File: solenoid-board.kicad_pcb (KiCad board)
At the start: 2 copper layers, 32.2 x 10.5 mm, 8 parts, among them J1 JST_PH, J2 0.1" header, Q1 FDN339AN

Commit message: Saved and quit kicad
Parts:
- moved D1 0.85 mm to (119.7, 106.2)
- moved C1 0.85 mm to (114.8, 106.5)
- moved G*** 0.85 mm to (113.5, 107.0)
- moved L1 0.85 mm to (122.5, 107.1)
- moved R1 0.81 mm to (108.9, 109.5)
- moved Q1 0.78 mm to (108.8, 104.9)
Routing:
- net GND: track 12.1 -> 9.70 mm
- net Net-(C1-Pad1): track 12.6 -> 14.7 mm
- net /FIRE!: track 5.46 -> 5.99 mm
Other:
- board size 32.2 x 10.5 mm -> 33 x 10.5 mm
- board text added: "git.io/pulsr"
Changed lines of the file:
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@@
   (general
     (thickness 1.6)
-    (drawings 11)
-    (tracks 29)
+    (drawings 12)
+    (tracks 26)
     (zones 0)
     (modules 8)
@@
   )
   (module graphics:kiwi10mm (layer B.Cu)
-    (at 112.7 107 180)
+    (at 113.55 107 180)
     (descr "Imported from kiwi.svg")
     (tags svg2mod)
@@
   )
   (module Capacitor_SMD:CP_Elec_6.3x5.4 (layer F.Cu)
-    (at 114 106.5 90)
+    (at 114.85 106.5 90)
     (descr "SMD capacitor, aluminum electrolytic, Panasonic C55, 6.3x5.4mm")
     (tags "capacitor electrolytic")
@@
   )
   (module Diode_SMD:D_SOD-123F (layer F.Cu)
-    (at 118.8 106.2 90)
+    (at 119.65 106.2 90)
     (descr D_SOD-123F)
     (tags D_SOD-123F)
@@
   )
   (module Connector_JST:JST_PH_S2B-PH-K_1x02_P2.00mm_Horizontal (layer F.Cu)
-    (at 121.7 107.1 90)
+    (at 122.55 107.1 90)
     (descr "JST PH series connector, S2B-PH-K (http://www.jst-mfg.com/product/pdf/eng/ePH.pdf), generated with kicad-footprint-generator")
     (tags "connector JST PH top entry")
@@
   )
   (module Package_TO_SOT_SMD:SOT-23_Handsoldering (layer F.Cu)
-    (at 108.3 105.5 90)
+    (at 108.8 104.9 90)
     (descr "SOT-23, Handsoldering")
     (tags SOT-23)
@@
   )
   (module Resistor_SMD:R_1206_3216Metric_Pad1.42x1.75mm_HandSolder (layer F.Cu)
-    (at 108.8 110.3 180)
+    (at 108.9 109.5 180)
     (descr "Resistor SMD 1206 (3216 Metric), square (rectangular) end terminal, IPC_7351 nominal with elongated pad for handsoldering. (Body size source: http://www.tortai-tech.com/upload/download/2011102023233369053.pdf), generated with kicad-footprint-generator")
     (tags "resistor handsolder")
     (attr smd)
-    (fp_text reference R1 (at 0 1.5) (layer F.SilkS)
-      (effects (font (size 1 1) (thickness 0.15)))
+    (fp_text reference R1 (at 0 1.4) (layer F.SilkS)
+      (effects (font (size 0.8 0.8) (thickness 0.13)))
     )
     (fp_text value 22R (at 0 1.82) (layer F.Fab)
@@
     )
   )
-  (gr_text Solenoid (at 121.4 102.9) (layer B.SilkS)
+  (gr_text git.io/pulsr (at 127.5 110) (layer B.SilkS)
+    (effects (font (size 1.25 1.25) (thickness 0.2)) (justify left mirror))
+  )
+  (gr_text Solenoid (at 122.25 102.9) (layer B.SilkS)
     (effects (font (size 1.5 1.5) (thickness 0.3)) (justify mirror))
   )
-  (gr_text "-\n+" (at 122.8 106.1) (layer B.SilkS)
+  (gr_text "-\n+" (at 123.65 106.1) (layer B.SilkS)
     (effects (font (size 1.2 1.2) (thickness 0.2)) (justify right mirror))
   )
-  (gr_arc (start 125.95 103.25) (end 127.95 103.25) (angle -90) (layer Edge.Cuts) (width 0.05))
-  (gr_arc (start 125.95 109.75) (end 125.95 111.75) (angle -90) (layer Edge.Cuts) (width 0.05))
+  (gr_arc (start 126.8 103.25) (end 128.8 103.25) (angle -90) (layer Edge.Cuts) (width 0.05))
+  (gr_arc (start 126.8 109.75) (end 126.8 111.75) (angle -90) (layer Edge.Cuts) (width 0.05))
   (gr_arc (start 97.8 109.75) (end 95.8 109.75) (angle -90) (layer Edge.Cuts) (width 0.05))
   (gr_arc (start 97.8 103.25) (end 97.8 101.25) (angle -90) (layer Edge.Cuts) (width 0.05))
@@
     (effects (font (size 1.2 1.2) (thickness 0.2)) (justify left mirror))
   )
-  (gr_line (start 125.95 101.25) (end 97.8 101.25) (layer Edge.Cuts) (width 0.05))
-  (gr_line (start 127.95 109.75) (end 127.95 103.25) (layer Edge.Cuts) (width 0.05))
-  (gr_line (start 97.8 111.75) (end 125.95 111.75) (layer Edge.Cuts) (width 0.05))
+  (gr_line (start 126.8 101.25) (end 97.8 101.25) (layer Edge.Cuts) (width 0.05))
+  (gr_line (start 128.8 109.75) (end 128.8 103.25) (layer Edge.Cuts) (width 0.05))
+  (gr_line (start 97.8 111.75) (end 126.8 111.75) (layer Edge.Cuts) (width 0.05))
   (gr_line (start 95.8 103.25) (end 95.8 109.75) (layer Edge.Cuts) (width 0.05))
-  (segment (start 114 109.3) (end 112.5 109.3) (width 0.6) (layer F.Cu) (net 1))
-  (segment (start 111.5 110.3) (end 110.3875 110.3) (width 0.6) (layer F.Cu) (net 1))
-  (segment (start 112.5 109.3) (end 111.5 110.3) (width 0.6) (layer F.Cu) (net 1))
-  (segment (start 117.1 109.3) (end 118.8 107.6) (width 1) (layer F.Cu) (net 1))
-  (segment (start 114 109.3) (end 117.1 109.3) (width 1) (layer F.Cu) (net 1))
-  (segment (start 119.3 107.1) (end 118.8 107.6) (width 1) (layer F.Cu) (net 1))
-  (segment (start 121.7 107.1) (end 119.3 107.1) (width 1) (layer F.Cu) (net 1))
+  (segment (start 114.85 109.3) (end 113.35 109.3) (width 0.6) (layer F.Cu) (net 1))
+  (segment (start 117.95 109.3) (end 119.65 107.6) (width 1) (layer F.Cu) (net 1))
+  (segment (start 114.85 109.3) (end 117.95 109.3) (width 1) (layer F.Cu) (net 1))
+  (segment (start 120.15 107.1) (end 119.65 107.6) (width 1) (layer F.Cu) (net 1))
+  (segment (start 122.55 107.1) (end 120.15 107.1) (width 1) (layer F.Cu) (net 1))
+  (segment (start 110.5875 109.3) (end 110.3875 109.5) (width 0.6) (layer F.Cu) (net 1))
+  (segment (start 114.85 109.3) (end 110.5875 109.3) (width 0.6) (layer F.Cu) (net 1))
   (segment (start 102.44 103.96) (end 101.9 104.5) (width 0.6) (layer F.Cu) (net 2))
   (segment (start 105 103.96) (end 102.44 103.96) (width 0.6) (layer F.Cu) (net 2))
-  (segment (start 108.26 103.96) (end 108.3 104) (width 0.6) (layer F.Cu) (net 2))
-  (segment (start 105.2 103.96) (end 108.26 103.96) (width 0.6) (layer F.Cu) (net 2))
-  (segment (start 113.7 104) (end 114 103.7) (width 0.8) (layer F.Cu) (net 2))
-  (segment (start 108.5 104) (end 113.7 104) (width 0.8) (layer F.Cu) (net 2))
-  (segment (start 119.9 104.975) (end 119.9 104.8) (width 0.8) (layer F.Cu) (net 3))
-  (segment (start 120.025 105.1) (end 119.9 104.975) (width 0.8) (layer F.Cu) (net 3))
-  (segment (start 121.7 105.1) (end 120.025 105.1) (width 0.8) (layer F.Cu) (net 3))
-  (segment (start 119.9 104.8) (end 118.8 104.8) (width 0.8) (layer F.Cu) (net 3))
-  (segment (start 117.25 104.8) (end 115.55 106.5) (width 1) (layer F.Cu) (net 3))
-  (segment (start 118.8 104.8) (end 117.25 104.8) (width 1) (layer F.Cu) (net 3))
-  (segment (start 110.85 107) (end 109.6 107) (width 1) (layer F.Cu) (net 3))
-  (segment (start 111.35 106.5) (end 110.85 107) (width 1) (layer F.Cu) (net 3))
-  (segment (start 115.55 106.5) (end 111.35 106.5) (width 1) (layer F.Cu) (net 3))
+  (segment (start 114.55 104) (end 114.85 103.7) (width 0.8) (layer F.Cu) (net 2))
+  (segment (start 114.85 103.7) (end 108.9 103.7) (width 1) (layer F.Cu) (net 2))
+  (segment (start 120.75 104.975) (end 120.75 104.8) (width 0.8) (layer F.Cu) (net 3))
+  (segment (start 120.875 105.1) (end 120.75 104.975) (width 0.8) (layer F.Cu) (net 3))
+  (segment (start 122.55 105.1) (end 120.875 105.1) (width 0.8) (layer F.Cu) (net 3))
+  (segment (start 120.75 104.8) (end 119.65 104.8) (width 0.8) (layer F.Cu) (net 3))
+  (segment (start 118.1 104.8) (end 116.4 106.5) (width 1) (layer F.Cu) (net 3))
+  (segment (start 119.65 104.8) (end 118.1 104.8) (width 1) (layer F.Cu) (net 3))
+  (segment (start 116.4 106.5) (end 112.2 106.5) (width 1) (layer F.Cu) (net 3))
+  (segment (start 112.2 106.5) (end 109.9 106.5) (width 1) (layer F.Cu) (net 3))
   (segment (start 101.9 106.5) (end 105 106.5) (width 0.4) (layer F.Cu) (net 4))
-  (segment (start 106.85 106.5) (end 107.35 107) (width 0.4) (layer F.Cu) (net 4))
-  (segment (start 105.2 106.5) (end 106.85 106.5) (width 0.4) (layer F.Cu) (net 4))
+  (segment (start 107.75 106.5) (end 107.85 106.4) (width 0.4) (layer F.Cu) (net 4))
+  (segment (start 105 106.5) (end 107.75 106.5) (width 0.4) (layer F.Cu) (net 4))
   (segment (start 104.46 108.5) (end 105 109.04) (width 0.6) (layer F.Cu) (net 5))
   (segment (start 101.9 108.5) (end 104.46 108.5) (width 0.6) (layer F.Cu) (net 5))
-  (segment (start 106.46 110.3) (end 105.2 109.04) (width 0.6) (layer F.Cu) (net 5))
-  (segment (start 107.2125 110.3) (end 106.46 110.3) (width 0.6) (layer F.Cu) (net 5))
+  (segment (start 105.46 109.5) (end 105 109.04) (width 0.6) (layer F.Cu) (net 5))
+  (segment (start 107.4125 109.5) (end 105.46 109.5) (width 0.6) (layer F.Cu) (net 5))
+  (zone (net 2) (net_name GND) (layer B.Cu) (hatch edge 0.508)
+    (connect_pads (clearance 0.5))
+    (min_thickness 0.25)
+    (fill yes (arc_segments 32) (thermal_gap 0.5) (thermal_bridge_width 0.5))
+    (polygon
+      (pts
+        (xy 95.75 101.25) (xy 128.8 101.25) (xy 128.8 111.75) (xy 95.75 111.75)
+      )
+    )
+  )
   (zone (net 2) (net_name GND) (layer F.Cu) (hatch edge 0.508)
     (connect_pads (clearance 0.5))
@@
     (polygon
       (pts
-        (xy 96.2 101.25) (xy 127.95 101.25) (xy 127.95 111.75) (xy 96.2 111.75)
+        (xy 95.75 101.25) (xy 128.8 101.25) (xy 128.8 111.75) (xy 95.75 111.75)
       )
     )
-  )
-  (zone (net 2) (net_name GND) (layer B.Cu) (hatch edge 0.508)
-    (connect_pads (clearance 0.5))
-    (min_thickness 0.25)
-    (fill yes (arc_segments 32) (thermal_gap 0.5) (thermal_bridge_width 0.5))
-    (polygon
-      (pts
-        (xy 96.2 101.25) (xy 127.95 101.25) (xy 127.95 111.75) (xy 96.2 111.75)
-      )
-    )

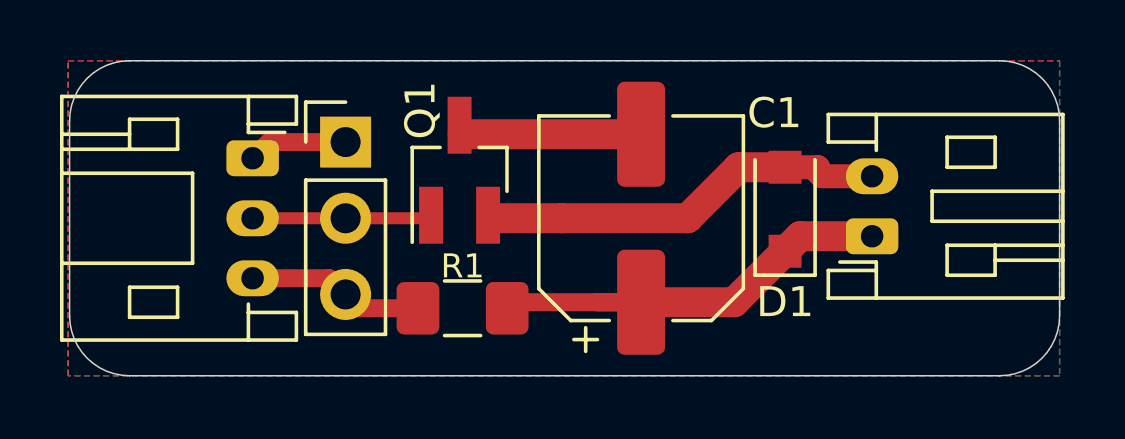
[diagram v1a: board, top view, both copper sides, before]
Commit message: Fixed mosfet pinout and added gate pulldown
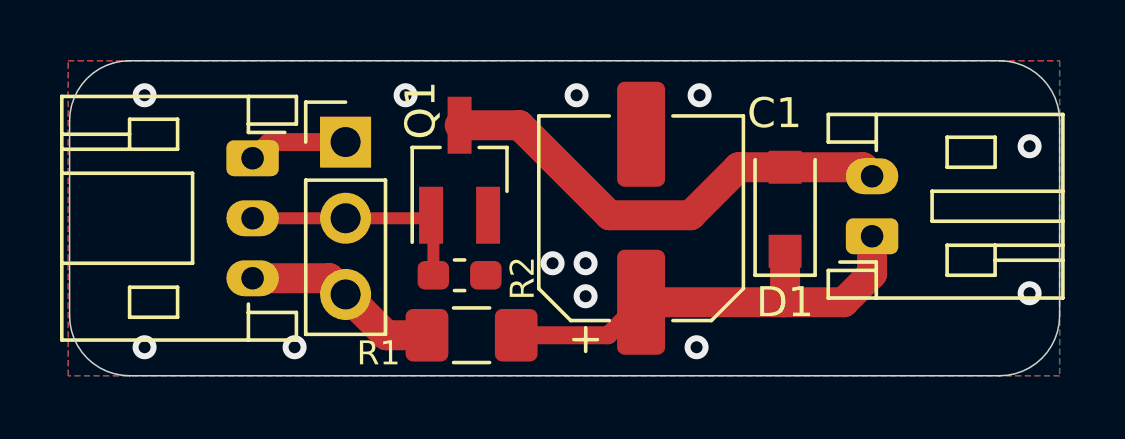
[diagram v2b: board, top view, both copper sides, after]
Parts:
- added R2: 10k, Resistor_SMD:R_0603_1608Metric_Pad1.05x0.95mm_HandSolder, F.Cu at (108.8, 108.4)
- moved R1 0.95 mm to (109.2, 110.4)
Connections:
- Q1 pad 2: Net-(D1-Pad2) -> GND
- Q1 pad 3: GND -> Net-(D1-Pad2)
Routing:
- net GND: track 9.70 -> 3.32 mm, vias 0 -> 12
- net Net-(D1-Pad2): track 13.6 -> 15.8 mm
- net /FIRE!: track 5.99 -> 8.02 mm
- net Net-(C1-Pad1): track 14.7 -> 15.7 mm
- net +5V: track 5.93 -> 6.60 mm
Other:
- board text added: "v1.0.1"
